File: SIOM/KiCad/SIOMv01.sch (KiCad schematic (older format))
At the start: 25 parts, among them J101 AnaOut01, J102 P1, J103 AnaOut2, J104 I2C 5V #1, J105 TMP01, J106 TMP02, J107 TMP03, J108 I2C 5V #2, J109 TMP04, J110 TMP05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

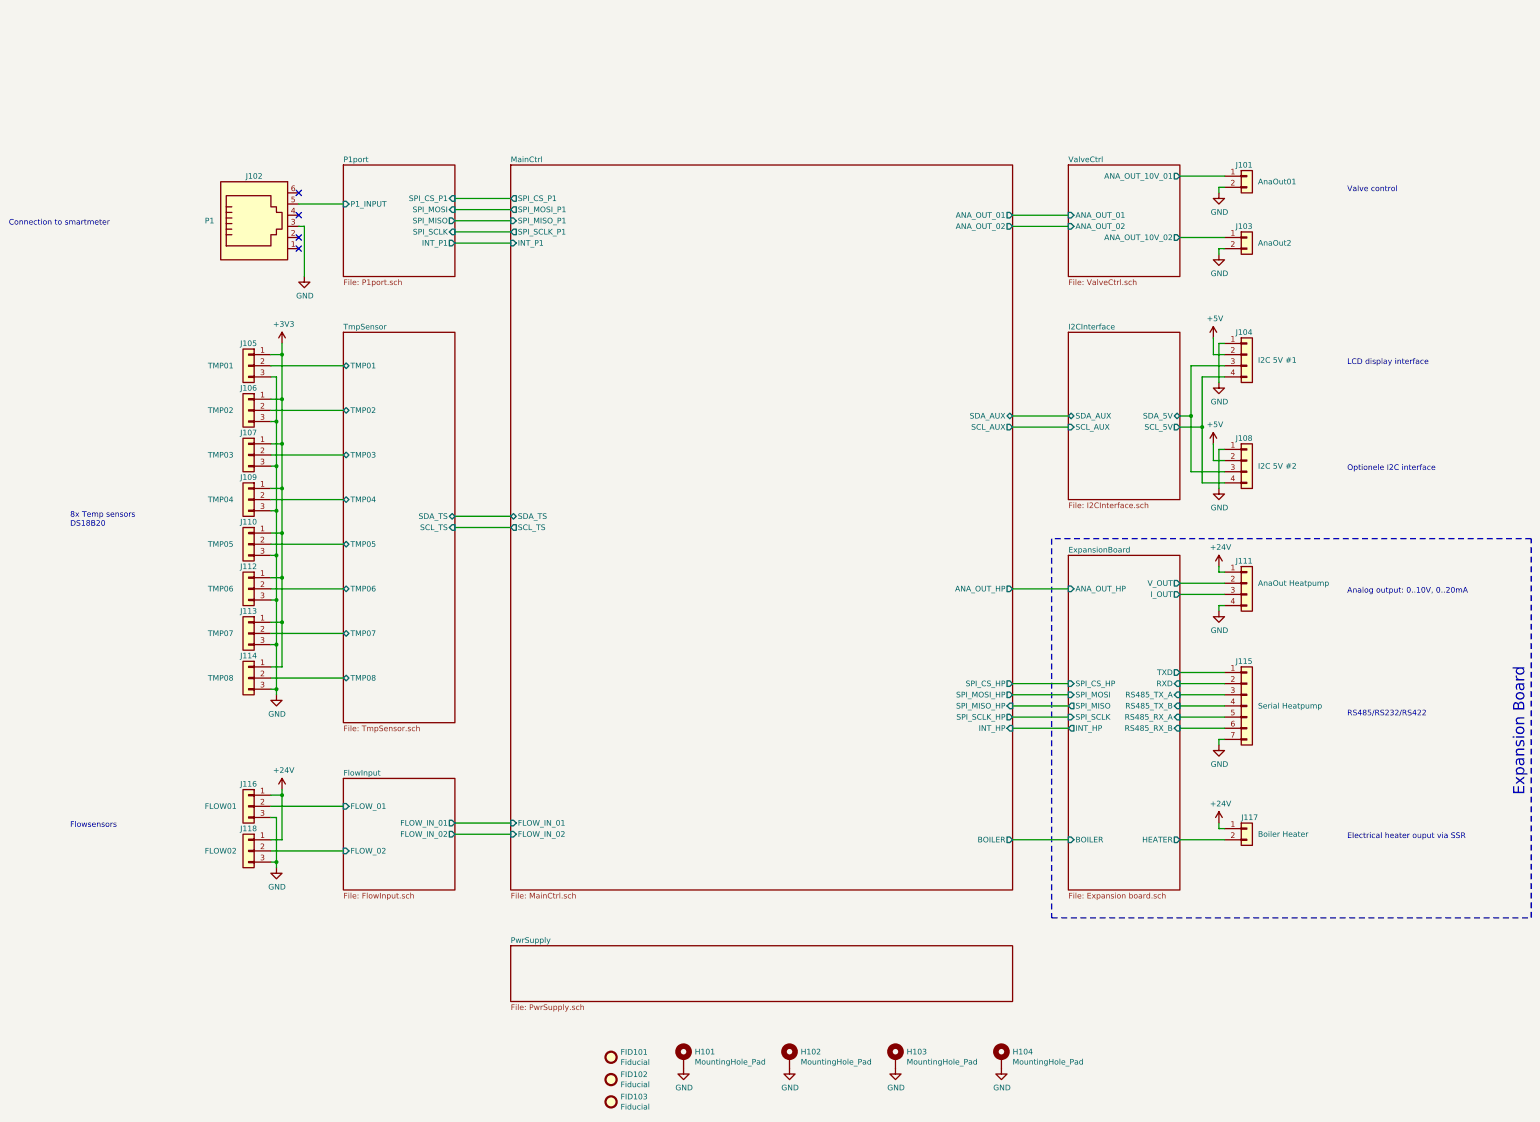
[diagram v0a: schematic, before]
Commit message: KiCad files SIOM_def
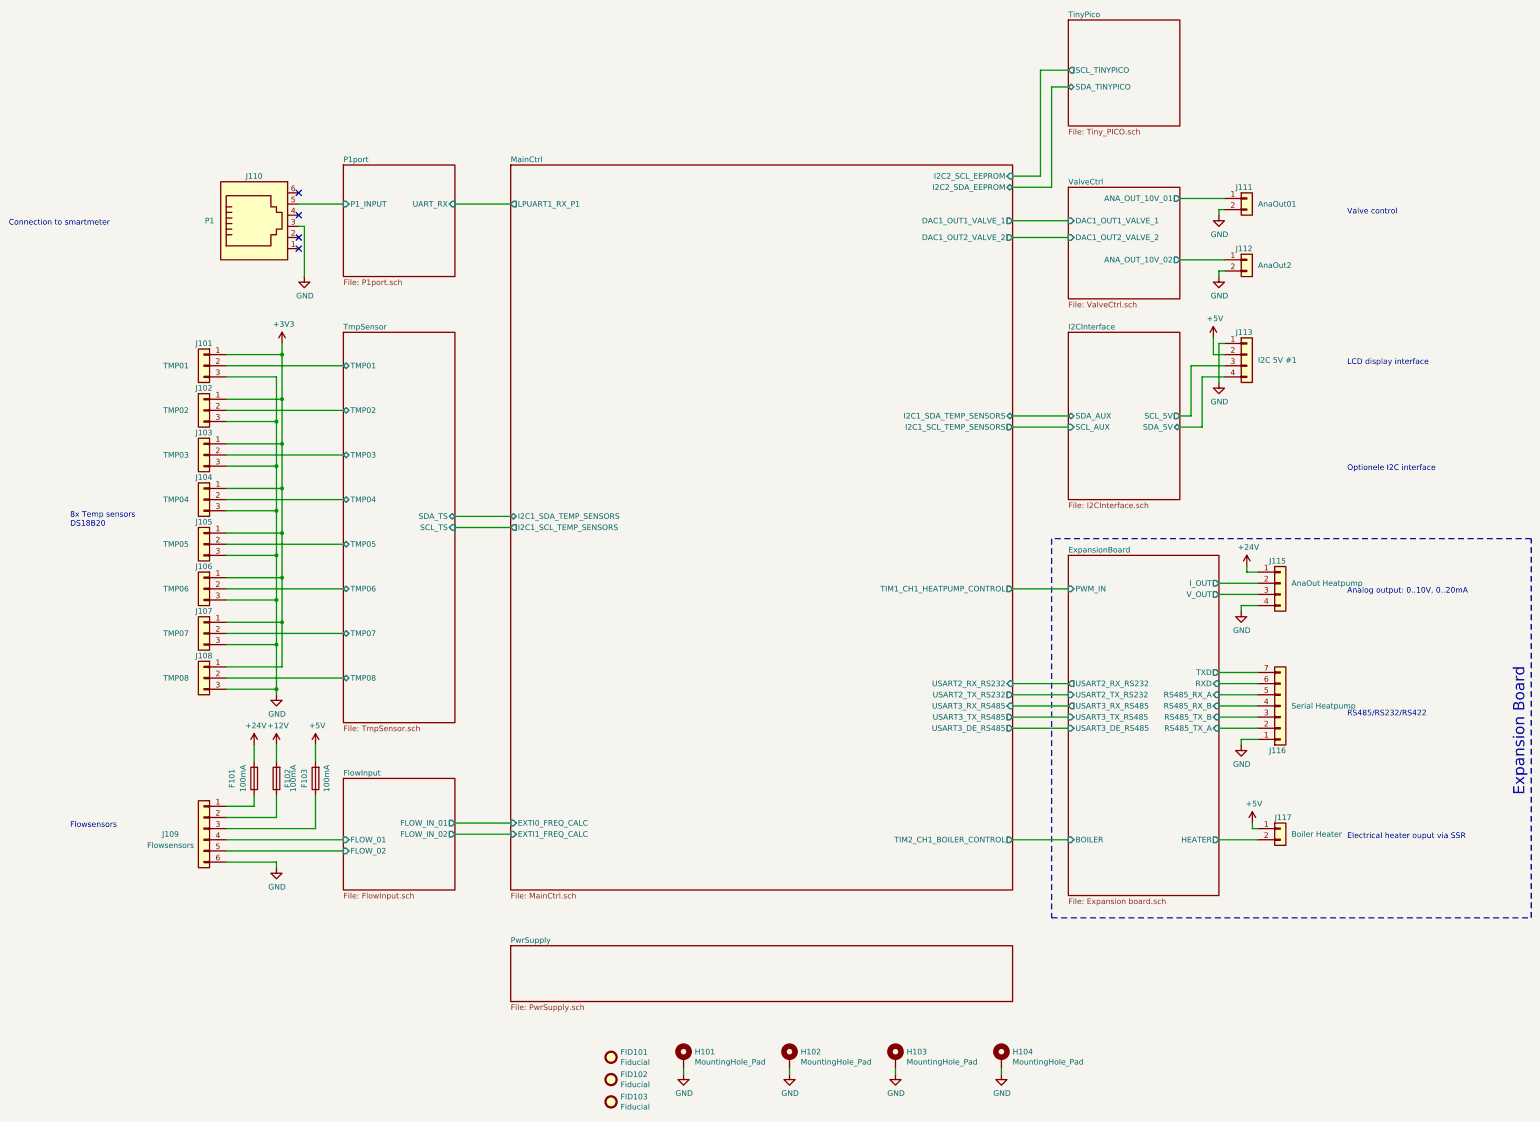
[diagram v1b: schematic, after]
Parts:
- removed J108: I2C 5V #2, Connector_PinHeader_2.54mm:PinHeader_1x04_P2.54mm_Vertical, symbol SIOMv01-rescue:Conn_01x04-Connector_Generic
- removed J116: FLOW01, Connector_PinHeader_2.54mm:PinHeader_1x03_P2.54mm_Vertical, symbol SIOMv01-rescue:Conn_01x03-Connector_Generic
- removed J118: FLOW02, Connector_PinHeader_2.54mm:PinHeader_1x03_P2.54mm_Vertical, symbol SIOMv01-rescue:Conn_01x03-Connector_Generic
- added F101, F102, F103: 100mA, Fuse:Fuse_1206_3216Metric_Pad1.42x1.75mm_HandSolder, symbol Device:Fuse
- added J109: Flowsensors, Connector_Phoenix_MC:PhoenixContact_MCV_1,5_6-G-3.81_1x06_P3.81mm_Vertical, symbol Connector_Generic:Conn_01x06
- J101: renamed from J105; footprint Connector_PinHeader_2.54mm:PinHeader_1x03_P2.54mm_Vertical -> Connector_Phoenix_MC:PhoenixContact_MCV_1,5_3-G-3.81_1x03_P3.81mm_Vertical
- J102: renamed from J106; footprint Connector_PinHeader_2.54mm:PinHeader_1x03_P2.54mm_Vertical -> Connector_Phoenix_MC:PhoenixContact_MCV_1,5_3-G-3.81_1x03_P3.81mm_Vertical
- J103: renamed from J107; footprint Connector_PinHeader_2.54mm:PinHeader_1x03_P2.54mm_Vertical -> Connector_Phoenix_MC:PhoenixContact_MCV_1,5_3-G-3.81_1x03_P3.81mm_Vertical
- J104: renamed from J109; footprint Connector_PinHeader_2.54mm:PinHeader_1x03_P2.54mm_Vertical -> Connector_Phoenix_MC:PhoenixContact_MCV_1,5_3-G-3.81_1x03_P3.81mm_Vertical
- J105: renamed from J110; footprint Connector_PinHeader_2.54mm:PinHeader_1x03_P2.54mm_Vertical -> Connector_Phoenix_MC:PhoenixContact_MCV_1,5_3-G-3.81_1x03_P3.81mm_Vertical
- J106: renamed from J112; footprint Connector_PinHeader_2.54mm:PinHeader_1x03_P2.54mm_Vertical -> Connector_Phoenix_MC:PhoenixContact_MCV_1,5_3-G-3.81_1x03_P3.81mm_Vertical
- J107: renamed from J113; footprint Connector_PinHeader_2.54mm:PinHeader_1x03_P2.54mm_Vertical -> Connector_Phoenix_MC:PhoenixContact_MCV_1,5_3-G-3.81_1x03_P3.81mm_Vertical
- J108: renamed from J114; footprint Connector_PinHeader_2.54mm:PinHeader_1x03_P2.54mm_Vertical -> Connector_Phoenix_MC:PhoenixContact_MCV_1,5_3-G-3.81_1x03_P3.81mm_Vertical
- J111: renamed from J101; footprint Connector_PinHeader_2.54mm:PinHeader_1x02_P2.54mm_Vertical -> Connector_Phoenix_MC:PhoenixContact_MCV_1,5_2-G-3.81_1x02_P3.81mm_Vertical
- J112: renamed from J103; footprint Connector_PinHeader_2.54mm:PinHeader_1x02_P2.54mm_Vertical -> Connector_Phoenix_MC:PhoenixContact_MCV_1,5_2-G-3.81_1x02_P3.81mm_Vertical
- J113: renamed from J104; footprint Connector_PinHeader_2.54mm:PinHeader_1x04_P2.54mm_Vertical -> Connector_Phoenix_MC:PhoenixContact_MCV_1,5_4-G-3.81_1x04_P3.81mm_Vertical
- J115: renamed from J111; footprint Connector_PinHeader_2.54mm:PinHeader_1x04_P2.54mm_Vertical -> Connector_Phoenix_MC:PhoenixContact_MCV_1,5_4-G-3.81_1x04_P3.81mm_Vertical
- J116: renamed from J115; footprint Connector_PinHeader_2.54mm:PinHeader_1x07_P2.54mm_Vertical -> Connector_Phoenix_MC:PhoenixContact_MCV_1,5_7-G-3.81_1x07_P3.81mm_Vertical
- J117: footprint Connector_PinHeader_2.54mm:PinHeader_1x02_P2.54mm_Vertical -> Connector_Phoenix_MC:PhoenixContact_MCV_1,5_2-G-3.81_1x02_P3.81mm_Vertical
- renumbered J102 to J110
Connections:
- net +24V: now also F101.2; no longer J117.1 (Pin_1)
- net +5V: now also J117.1 (Pin_1), F103.2
- net ExpansionBoard/I_OUT: now also J115.2 (Pin_2); no longer J115.3 (Pin_3)
- net ExpansionBoard/RS485_RX_B: now also J116.4 (Pin_4); no longer J116.6 (Pin_6)
- net ExpansionBoard/RS485_TX_A: now also J116.2 (Pin_2); no longer J116.3 (Pin_3)
- net ExpansionBoard/RS485_TX_B: now also J116.3 (Pin_3); no longer J116.4 (Pin_4)
- net ExpansionBoard/RXD: now also J116.6 (Pin_6); no longer J116.2 (Pin_2)
- net ExpansionBoard/TXD: now also J116.7 (Pin_7); no longer J116.1 (Pin_1)
- net ExpansionBoard/V_OUT: now also J115.3 (Pin_3); no longer J115.2 (Pin_2)
- net FlowInput/FLOW_01: now also J109.4 (Pin_4)
- net FlowInput/FLOW_02: now also J109.5 (Pin_5)
- net GND: now also J116.1 (Pin_1), J109.6 (Pin_6); no longer J116.7 (Pin_7)
- net I2CInterface/SCL_5V: now also J113.3 (Pin_3); no longer J113.4 (Pin_4)
- net I2CInterface/SDA_5V: now also J113.4 (Pin_4); no longer J113.3 (Pin_3)
- new net: F103.1, J109.3 (Pin_3)
- new net: F102.1, J109.2 (Pin_2)
- new net: F101.1, J109.1 (Pin_1)
- new net +12V: F102.2
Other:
- moved on the sheet: J101, J102, J103, J104, J105, J106, J107, J108, J111, J112, J115, J116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
